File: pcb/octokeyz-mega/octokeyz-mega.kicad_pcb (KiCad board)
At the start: 2 copper layers, 84.6 x 79.8 mm, 37 parts, among them J1 USB_B_Mini, J2 PIN H 5P, J3 PIN S 4P, SW1 Gateron KS-3, SW2 Gateron KS-3, SW3 Gateron KS-3, SW4 Gateron KS-3, SW5 Gateron KS-3, SW6 Gateron KS-3, SW7 Gateron KS-3, SW8 Gateron KS-3, U1 USBLC6-2SC6, U2 MCP1700-3302E, U3 STM32F042K6T6

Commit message: pcb: octokeyz-mega: revision 20240601
minor changes.
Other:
- board text added: "+3.3V"
- board text added: "+3.3V OUT. ONLY!"
- board text added: "Boot to DFU"
- board text added: "GND"
- board text added: "NRST"
- board text added: "OLED"
- board text added: "SCL"
- board text added: "SDA"
- board text added: "SWCLK"
- board text added: "SWD"
- board text added: "SWDIO"
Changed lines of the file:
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@@
 			(layer "F.Fab")
 		)
-		(fp_text user "GND"
-			(at 2.007 -0.01 0)
-			(unlocked yes)
-			(layer "F.SilkS")
-			(effects
-				(font
-					(size 0.6 0.6)
-					(thickness 0.15)
-				)
-			)
-		)
-		(fp_text user "+3.3v"
-			(at 2.007 2.53 0)
-			(unlocked yes)
-			(layer "F.SilkS")
-			(effects
-				(font
-					(size 0.6 0.6)
-					(thickness 0.15)
-				)
-			)
-		)
-		(fp_text user "SDA"
-			(at 2.007 7.61 0)
-			(unlocked yes)
-			(layer "F.SilkS")
-			(effects
-				(font
-					(size 0.6 0.6)
-					(thickness 0.15)
-				)
-			)
-		)
-		(fp_text user "OLED"
-			(at 0.991 10.277 0)
-			(unlocked yes)
-			(layer "F.SilkS")
-			(effects
-				(font
-					(size 0.6 0.6)
-					(thickness 0.15)
-				)
-			)
-		)
-		(fp_text user "SCL"
-			(at 2.007 5.07 0)
-			(unlocked yes)
-			(layer "F.SilkS")
-			(effects
-				(font
-					(size 0.6 0.6)
-					(thickness 0.15)
-				)
-			)
-		)
 		(fp_text user "${REFERENCE}"
 			(at 0 3.81 0)
@@
 		(tags "Through hole angled pin header THT 1x05 2.54mm single row")
 		(property "Reference" "J2"
-			(at 1.27 3.175 0)
+			(at 2.794 3.175 0)
 			(layer "B.SilkS")
 			(effects
@@
 					(thickness 0.15)
 				)
-				(justify mirror)
+				(justify right mirror)
 			)
 		)
@@
 			(layer "B.Fab")
 		)
-		(fp_text user "NRST"
-			(at 8.89 -9.271 0)
-			(unlocked yes)
-			(layer "B.SilkS")
-			(effects
-				(font
-					(size 0.6 0.6)
-					(thickness 0.15)
-				)
-				(justify mirror)
-			)
-		)
-		(fp_text user "SWD"
-			(at 1.27 2.032 0)
-			(unlocked yes)
-			(layer "B.SilkS")
-			(effects
-				(font
-					(size 0.6 0.6)
-					(thickness 0.15)
-				)
-				(justify mirror)
-			)
-		)
-		(fp_text user "SWDIO"
-			(at 8.763 -6.731 0)
-			(unlocked yes)
-			(layer "B.SilkS")
-			(effects
-				(font
-					(size 0.6 0.6)
-					(thickness 0.15)
-				)
-				(justify mirror)
-			)
-		)
-		(fp_text user "SWCLK"
-			(at 8.636 -1.651 0)
-			(unlocked yes)
-			(layer "B.SilkS")
-			(effects
-				(font
-					(size 0.6 0.6)
-					(thickness 0.15)
-				)
-				(justify mirror)
-			)
-		)
-		(fp_text user "+3.3v"
-			(at 8.763 0.889 0)
-			(unlocked yes)
-			(layer "B.SilkS")
-			(effects
-				(font
-					(size 0.6 0.6)
-					(thickness 0.15)
-				)
-				(justify mirror)
-			)
-		)
-		(fp_text user "GND"
-			(at 9.271 -4.191 0)
-			(unlocked yes)
-			(layer "B.SilkS")
-			(effects
-				(font
-					(size 0.6 0.6)
-					(thickness 0.15)
-				)
-				(justify mirror)
-			)
-		)
 		(fp_text user "${REFERENCE}"
 			(at 2.77 -5.08 90)
@@
 		(tags "Through hole angled pin header THT 1x02 2.54mm single row")
 		(property "Reference" "JP1"
-			(at 2.794 3.17 0)
+			(at 1.27 3.17 0)
 			(layer "B.SilkS")
 			(effects
@@
 					(thickness 0.15)
 				)
-				(justify mirror)
+				(justify left mirror)
 			)
 		)
@@
 			(layer "B.Fab")
 		)
-		(fp_text user "Boot to DFU"
-			(at 4.191 2.027 0)
-			(unlocked yes)
-			(layer "B.SilkS")
-			(effects
-				(font
-					(size 0.6 0.6)
-					(thickness 0.15)
-				)
-				(justify mirror)
-			)
-		)
 		(fp_text user "${REFERENCE}"
 			(at 2.77 -1.27 90)
@@
 		(layer "Edge.Cuts")
 	)
+	(gr_text "Boot to DFU"
+		(at 163.957 84.455 0)
+		(layer "B.SilkS")
+		(effects
+			(font
+				(size 0.6 0.6)
+				(thickness 0.15)
+			)
+			(justify left mirror)
+		)
+	)
+	(gr_text "SWCLK"
+		(at 155.067 69.088 0)
+		(layer "B.SilkS")
+		(effects
+			(font
+				(size 0.6 0.6)
+				(thickness 0.15)
+			)
+			(justify right mirror)
+		)
+	)
+	(gr_text "SWDIO"
+		(at 155.067 74.168 0)
+		(layer "B.SilkS")
+		(effects
+			(font
+				(size 0.6 0.6)
+				(thickness 0.15)
+			)
+			(justify right mirror)
+		)
+	)
+	(gr_text "+3.3V\nOUT. ONLY!"
+		(at 155.067 66.04 0)
+		(layer "B.SilkS")
+		(effects
+			(font
+				(size 0.6 0.6)
+				(thickness 0.15)
+			)
+			(justify right mirror)
+		)
+	)
 	(gr_text "Rev: ${REVISION}"
 		(at 132.461 137.795 0)
@@
 		)
 	)
+	(gr_text "SWD"
+		(at 162.433 65.405 0)
+		(layer "B.SilkS")
+		(effects
+			(font
+				(size 0.6 0.6)
+				(thickness 0.15)
+			)
+			(justify right mirror)
+		)
+	)
+	(gr_text "NRST"
+		(at 155.067 76.708 0)
+		(layer "B.SilkS")
+		(effects
+			(font
+				(size 0.6 0.6)
+				(thickness 0.15)
+			)
+			(justify right mirror)
+		)
+	)
+	(gr_text "GND"
+		(at 155.067 71.628 0)
+		(layer "B.SilkS")
+		(effects
+			(font
+				(size 0.6 0.6)
+				(thickness 0.15)
+			)
+			(justify right mirror)
+		)
+	)
+	(gr_text "OLED"
+		(at 180.721 64.262 0)
+		(layer "F.SilkS")
+		(effects
+			(font
+				(size 0.6 0.6)
+				(thickness 0.15)
+			)
+		)
+	)
+	(gr_text "SCL"
+		(at 175.514 63.246 0)
+		(layer "F.SilkS")
+		(effects
+			(font
+				(size 0.6 0.6)
+				(thickness 0.15)
+			)
+		)
+	)
+	(gr_text "GND"
+		(at 170.434 63.246 0)
+		(layer "F.SilkS")
+		(effects
+			(font
+				(size 0.6 0.6)
+				(thickness 0.15)
+			)
+		)
+	)
 	(gr_text "octokeyz.rgm.io"
 		(at 132.461 96.266 0)
@@
 			)
 		)
+	)
+	(gr_text "+3.3V"
+		(at 172.974 63.246 0)
+		(layer "F.SilkS")
+		(effects
+			(font
+				(size 0.6 0.6)
+				(thickness 0.15)
+			)
+		)
+	)
+	(gr_text "SDA"
+		(at 178.054 63.246 0)
+		(layer "F.SilkS")
+		(effects
+			(font
+				(size 0.6 0.6)
+				(thickness 0.15)
+			)
+		)

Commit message: pcb: added STM32F042K4T6 as microcontroller alternative
as this is a purely cosmetic change that doesn't affects the produced
boards I do not bumped revision number neither re-generated gerber
files.
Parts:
- U3: value STM32F042K6T6 -> STM32F042K4T6 or STM32F042K6T6

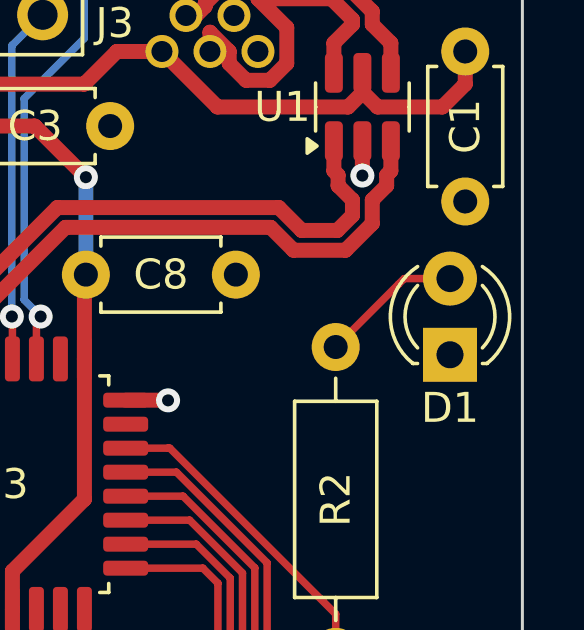
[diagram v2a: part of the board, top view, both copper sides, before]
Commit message: pcb: upgrade to kicad 9
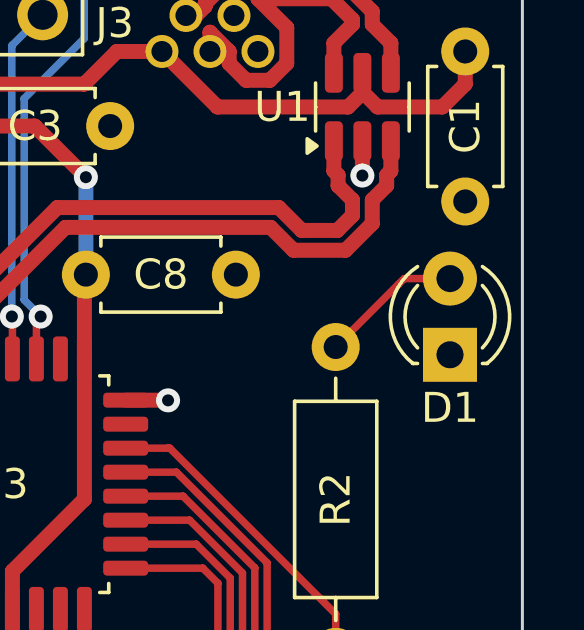
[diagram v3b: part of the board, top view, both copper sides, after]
